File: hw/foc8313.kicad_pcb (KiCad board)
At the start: 4 copper layers, 35 x 35 mm, 146 parts, among them J1 Tag Connect, J2 Encoder, J3 CAN, J4 CAN, J6 GPIO, SW1 SW_SPST, SW2 SW_SPST, U1 LMR36015SFBRNXR, U12 TJA1051TK/3,118, U2 XC6206P332MR, U3 DRV8313PWP, U4 STM32F103CBTx, U5 AS5047D, U6 ZD24C08AE1-STGMT, U7 INA240A2D, U8 INA240A2D, X1 X322516MLB4SI

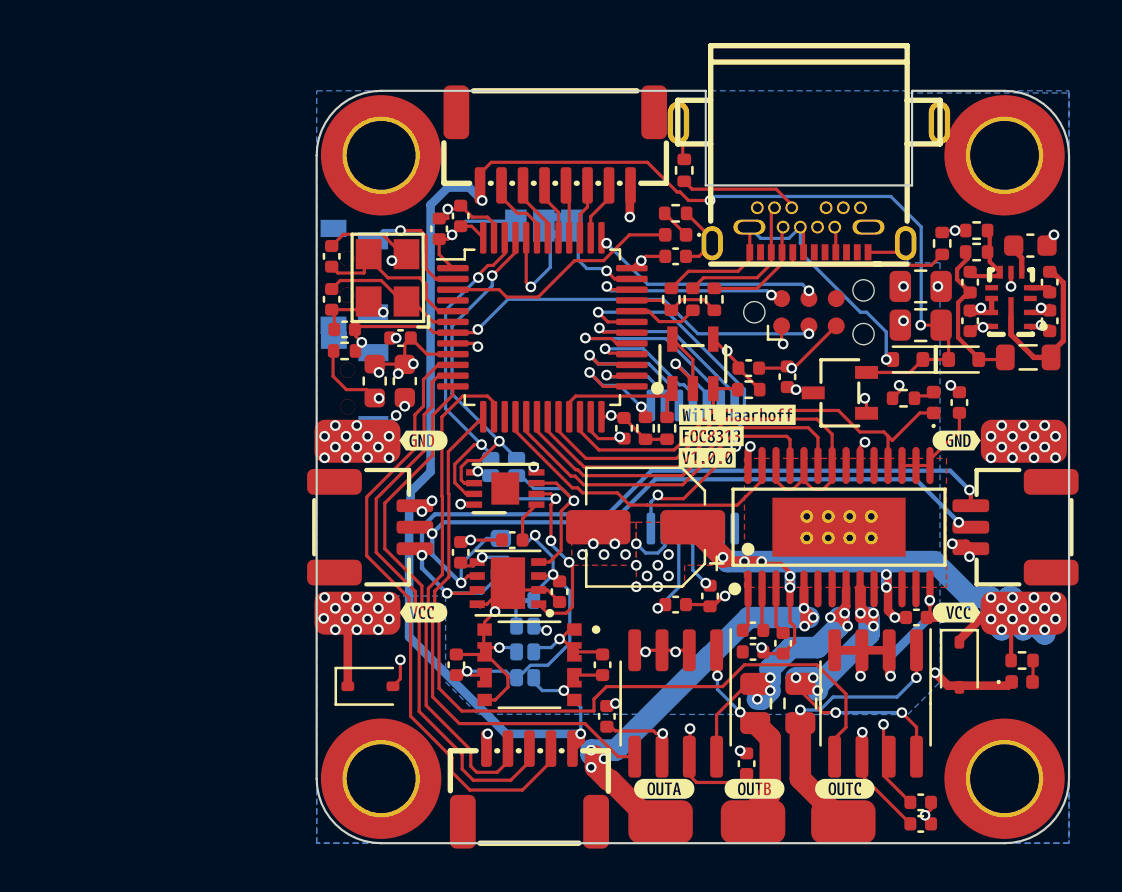
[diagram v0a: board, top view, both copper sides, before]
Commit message: [Hw] All connections completed - only DRC left
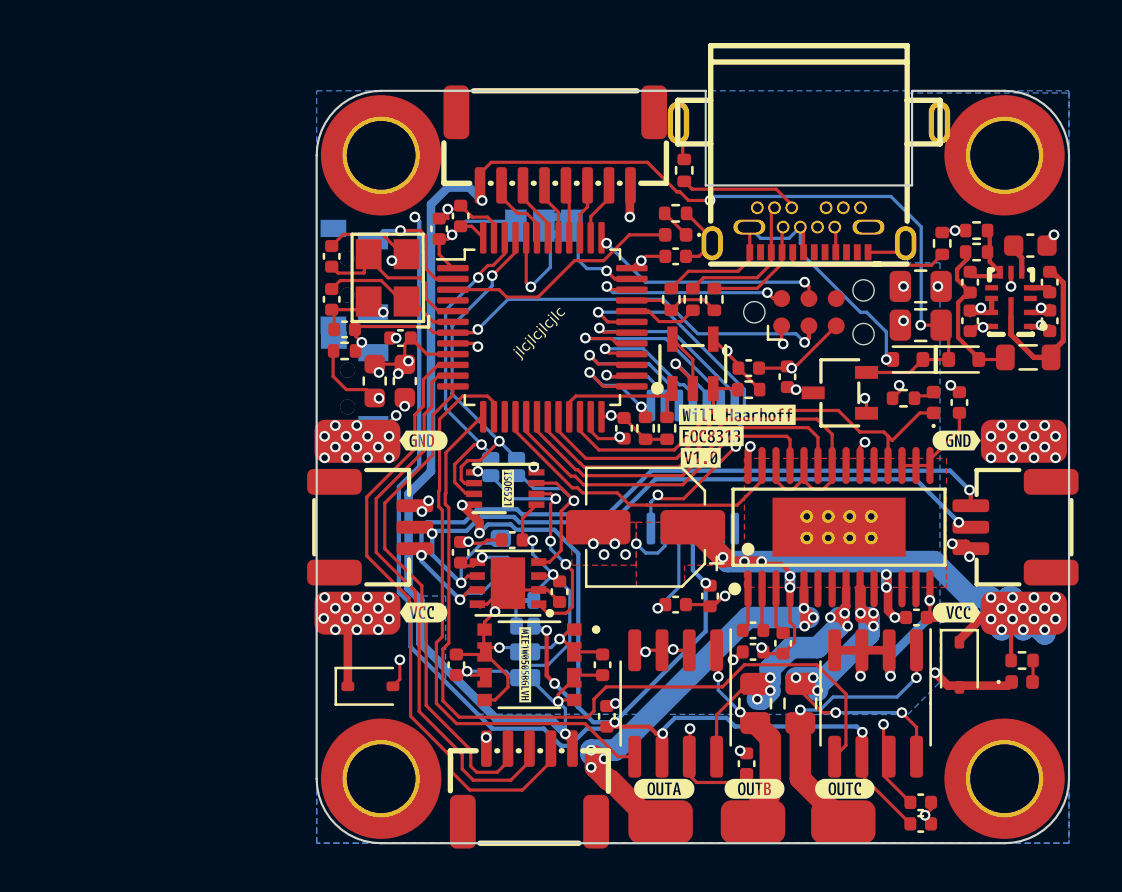
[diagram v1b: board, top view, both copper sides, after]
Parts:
- removed kibuzzard-66359B89: G***, kibuzzard-66359B89
- added kibuzzard-6635FB63: G***, kibuzzard-6635FB63, B.Cu at (133.5, 115.8)
- added kibuzzard-6635FB77: G***, kibuzzard-6635FB77, B.Cu at (132.5, 115.8)
- added kibuzzard-6635FB7E: G***, kibuzzard-6635FB7E, B.Cu at (131.5, 115.8)
- added kibuzzard-6635FC0D: G***, kibuzzard-6635FC0D, B.Cu at (156.0, 105.4)
- added kibuzzard-6635FC0D: G***, kibuzzard-6635FC0D, B.Cu at (123.9, 105.4)
- added kibuzzard-6635FC16: G***, kibuzzard-6635FC16, B.Cu at (124.1, 100.2)
- added kibuzzard-6635FC16: G***, kibuzzard-6635FC16, B.Cu at (156.0, 100.2)
- added kibuzzard-6635FD18: G***, kibuzzard-6635FD18, F.Cu at (140.4, 99.6)
- added kibuzzard-663606F1: G***, kibuzzard-663606F1, F.Cu at (132.2, 109.2)
- added kibuzzard-6636082D: G***, kibuzzard-6636082D, F.Cu at (131.4, 101.0)
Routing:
- net +3.3V: track 35.7 -> 108.5 mm, vias 12 -> 16
- net +5V: track 75.5 -> 74.5 mm
- net /~{NRST}: track 24.6 -> 25.4 mm
- net GND: track 80.1 -> 80.7 mm
- net VCC: vias 47 -> 40
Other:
- board text added: "Version 1.0"
- board text added: "jlcjlcjlcjlc"
- board text removed: "Version 1.0.0"

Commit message: [Hw] Optimised components for JLC basic parts
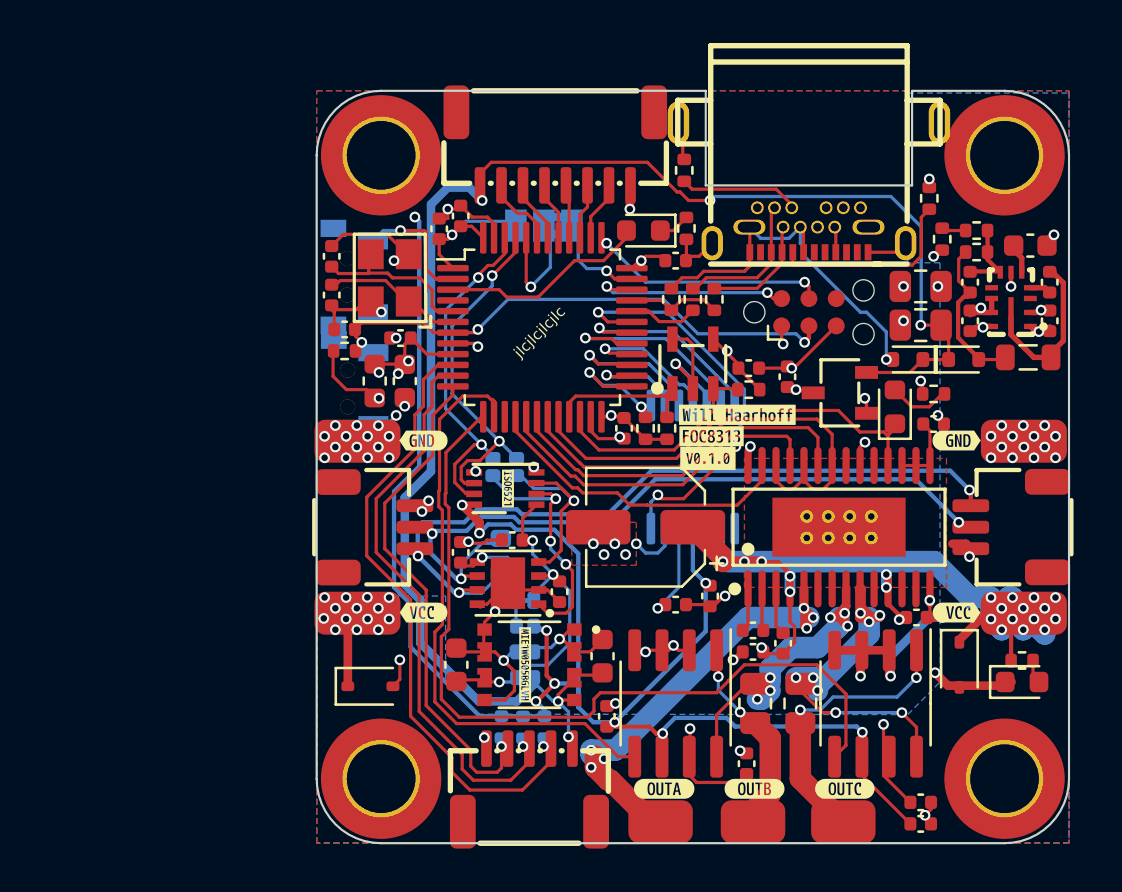
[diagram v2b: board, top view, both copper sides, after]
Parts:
- removed kibuzzard-6635FD18: G***, kibuzzard-6635FD18
- added R18: 4.7k, Resistor_SMD:R_0402_1005Metric, F.Cu at (153.2, 89.0)
- added R19: 5.1k, Resistor_SMD:R_0402_1005Metric, B.Cu at (133.1, 112.1)
- added R20: 5.1k, Resistor_SMD:R_0402_1005Metric, B.Cu at (132.1, 112.1)
- added R21: 5.1k, Resistor_SMD:R_0402_1005Metric, B.Cu at (131.1, 112.1)
- added kibuzzard-667F5C34: G***, kibuzzard-667F5C34, F.Cu at (140.7, 99.6)
- C13: value 5.1p -> 4.7p
- C37, C38: value 22uF -> 22u; footprint Capacitor_SMD:C_0402_1005Metric -> Capacitor_SMD:C_0603_1608Metric
- C8: value 470n -> 220n
- D4: footprint Diode_SMD:D_0402_1005Metric -> Diode_SMD:D_0603_1608Metric
- D5: value BLUE -> WHITE; footprint LED_SMD:LED_0402_1005Metric -> LED_SMD:LED_0603_1608Metric
- D7: value GREEN -> YELLOW; footprint LED_SMD:LED_0402_1005Metric -> LED_SMD:LED_0603_1608Metric
- R4: value 24.9k -> 20k
- U10: value ~ -> ISO6521
- moved R14 2.18 mm to (151.0, 87.5)
- moved D4 1.81 mm to (149.4, 97.2)
- moved R4 1.65 mm to (151.6, 89.4), turned to -90 degrees
- moved C8 1.56 mm to (151.2, 98.0), turned to 0 degrees
- moved D5 1.51 mm to (137.7, 89.0)
- moved R6 1.41 mm to (151.2, 96.6)
- moved R8 0.86 mm to (139.7, 88.9), turned to -90 degrees
- moved C37 0.40 mm to (135.8, 108.8)
- moved C16 0.20 mm to (123.2, 92.0)
- moved C3 0.20 mm to (139.2, 90.4)
- moved X1 0.10 mm to (125.9, 91.2)
- moved JP6 0.10 mm to (130.7, 100.0)
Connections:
- R4 pad 1: Net-(U1-FB) -> Net-(R18-Pad2)
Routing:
- net /~{DRV_NFAULT}: track 22.1 -> 20.1 mm
- net Net-(D4-A): track 1.07 -> 3.02 mm
- net /STATUS: track 11.2 -> 9.55 mm
- net +3.3V: track 108.5 -> 107.1 mm, vias 16 -> 17
- net Net-(USB1-CC1): track 7.72 -> 9.04 mm
- net +5V: track 74.5 -> 73.2 mm
- net GND: track 80.7 -> 82.0 mm, vias 71 -> 73
- net /PHC: track 19.7 -> 21.0 mm
- net /ENC2_A: track 28.7 -> 29.8 mm, vias 0 -> 1
- net /~{DRV_NRST}: track 4.32 -> 3.36 mm
- net Net-(R18-Pad2): track 0.00 -> 0.94 mm
- net /ENC2_B: track 26.1 -> 27.0 mm, vias 0 -> 1
- net /isocan/ISO5V: track 17.6 -> 16.8 mm
- net /ENC2_Z: track 23.3 -> 24.0 mm, vias 0 -> 1
- net /CAN.GND: track 19.9 -> 20.1 mm, vias 8 -> 7
- removed copper zone on F.Cu, net VCC
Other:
- board text added: "Version 0.1.0"
- board text removed: "Version 1.0"

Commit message: [Hw] Version 0.1.0 - sent for manufacture
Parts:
- added R22: 5.1k, Resistor_SMD:R_0402_1005Metric, B.Cu at (132.7, 94.6)
- added R23: 5.1k, Resistor_SMD:R_0402_1005Metric, B.Cu at (132.7, 95.6)
- added R24: 5.1k, Resistor_SMD:R_0402_1005Metric, B.Cu at (132.7, 93.6)
- SW1, SW2: footprint easyeda:SW-SMD_L4.7-W3.5-P3.35-EH -> easyeda:SW-TH_PANASONIC_EVPAKE31A
- U10: value ISO6521 -> ISO6521F
- moved kibuzzard-66359642 2.07 mm to (127.7, 94.1)
- moved kibuzzard-6635961B 1.97 mm to (127.4, 89.4)
- moved C7 1.43 mm to (123.5, 95.0)
- moved R1 1.43 mm to (123.5, 96.0)
- moved SW2 1.07 mm to (124.0, 95.3)
- moved SW1 0.69 mm to (124.0, 90.5)
- moved C16 0.67 mm to (123.5, 91.4), turned to 0 degrees
- moved C2 0.32 mm to (128.2, 88.6)
- moved C17 0.30 mm to (123.5, 90.2), turned to 180 degrees
- moved R7 0.20 mm to (155.3, 108.8)
- moved C26 0.20 mm to (150.4, 116.6)
- moved C27 0.20 mm to (150.4, 115.6)
- moved X1 0.20 mm to (126.1, 91.2)
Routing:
- net GND: track 82.0 -> 86.5 mm, vias 73 -> 75
- net +3.3V: track 107.1 -> 110.4 mm, vias 17 -> 22
- net /ENC1_A: track 9.71 -> 12.7 mm
- net /ENC1_Z: track 19.3 -> 22.0 mm
- net /ENC1_B: track 10.2 -> 12.6 mm
- net +3.3VA: track 14.3 -> 16.0 mm
- net +5V: track 73.2 -> 74.7 mm
- net /HSE_IN: track 7.83 -> 6.79 mm
- net /HSE_OUT: track 6.54 -> 5.87 mm
- net /~{BTN}: track 5.84 -> 6.45 mm
- net /CAN.GND: vias 7 -> 8

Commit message: [Hw] WIP begun revisions for v0.2.0
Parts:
- removed D2: RB521S30T1G, Diode_SMD:D_SOD-523
- added R25: 100k, Resistor_SMD:R_0402_1005Metric, F.Cu at (114.5, 98.0)
- added R26: 10k, Resistor_SMD:R_0402_1005Metric, F.Cu at (114.5, 100.0)
- C13: value 4.7p -> 100n
- R12, R13: value 6m -> 10m
- moved C13 43.4 mm to (111.5, 104.6), turned to 0 degrees
- moved D6 4.34 mm to (152.1, 91.2)
- moved C9 3.20 mm to (150.6, 94.8)
- moved L2 1.40 mm to (154.2, 95.0)
- moved C14 0.60 mm to (150.6, 92.8)
- moved C11 0.30 mm to (152.9, 92.9)
- moved J1 0.20 mm to (145.4, 93.0)
- turned C12 to 90 degrees
- turned C15 to 180 degrees
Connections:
- C12 pad 1: Net-(U1-SW) -> Net-(U1-NC)
- C13 pad 1: Net-(D2-A) -> /VSENSE
- C13 pad 2: Net-(U1-FB) -> GND
- C33 pad 2: /CAN.GND -> Net-(U12-EP)
- C34 pad 2: /CAN.GND -> Net-(U12-EP)
- C35 pad 2: /CAN.GND -> Net-(U12-EP)
- C38 pad 2: /CAN.GND -> Net-(U12-EP)
- J1 pad 1: +3V3 -> +3.3V
- L2 pad 1: Net-(D2-A) -> +5V
- L2 pad 2: Net-(U1-SW) -> Net-(U1-NC)
- PS1 pad 2: /CAN.GND -> Net-(U12-EP)
- PS1 pad 3_4: /CAN.GND -> Net-(U12-EP)
- PS1 pad 7: /CAN.GND -> unconnected-(PS1-VSEL-Pad7)
- R3 pad 1: Net-(D2-A) -> +5V
- U1 pad 12: Net-(U1-SW) -> Net-(U1-NC)
- U1 pad 3: unconnected-(U1-NC-Pad3) -> Net-(U1-NC)
- U10 pad 4: /CAN.GND -> Net-(U12-EP)
- U12 pad 2: /CAN.GND -> Net-(U12-EP)
- U12 pad 8: /CAN.GND -> Net-(U12-EP)
- U12 pad 9: /CAN.GND -> Net-(U12-EP)
- U2 pad 2: +5V -> +3.3V
- U2 pad 3: +3.3V -> +5V
- U4 pad 15: unconnected-(U4-PA5-Pad15) -> /VSENSE
- USB1 pad A10: /USB_DM_EXT -> unconnected-(USB1-SSRXN2-PadA10)
- USB1 pad A12: +5VD -> GND
- USB1 pad A4: GND -> +5VD
- USB1 pad A5: unconnected-(USB1-SSTXP1-PadA5) -> Net-(USB1-CC1)
- USB1 pad A6: unconnected-(USB1-SSTXN1-PadA6) -> /USB_DP_EXT
- USB1 pad A7: +5VD -> /USB_DM_EXT
- USB1 pad A8: Net-(USB1-CC1) -> unconnected-(USB1-SBU1-PadA8)
- USB1 pad A9: /USB_DP_EXT -> +5VD
- USB1 pad B1: +5VD -> GND
- USB1 pad B11: GND -> unconnected-(USB1-SSRXP1-PadB11)
- USB1 pad B12: unconnected-(USB1-SSRXN1-PadB12) -> GND
- USB1 pad B3: /USB_DM_EXT -> unconnected-(USB1-SSTXN2-PadB3)
- USB1 pad B4: /USB_DP_EXT -> +5VD
- USB1 pad B6: +5VD -> /USB_DP_EXT
- USB1 pad B7: unconnected-(USB1-SSTXN2-PadB7) -> /USB_DM_EXT
- USB1 pad B9: GND -> +5VD
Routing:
- net /CAN.GND: track 20.1 -> 3.60 mm, vias 8 -> 4
- net Net-(U12-EP): track 0.00 -> 11.7 mm, vias 0 -> 3
- net Net-(U1-SW): track 7.77 -> 0.00 mm
- net Net-(D2-A): track 7.14 -> 0.00 mm
- net Net-(USB1-CC2): track 5.45 -> 0.52 mm
- net Net-(U1-NC): track 0.00 -> 4.92 mm
- net GND: track 86.5 -> 90.4 mm, vias 75 -> 74
- net VCC: track 52.9 -> 56.4 mm, vias 40 -> 41
- net +3.3V: track 110.4 -> 112.9 mm, vias 22 -> 20
- net /USB_DP_EXT: track 5.35 -> 7.71 mm, vias 0 -> 1
- net +5VD: track 17.9 -> 20.1 mm
- net /SWDIO: track 9.59 -> 11.4 mm
- net +5V: track 74.7 -> 76.5 mm, vias 5 -> 6
- net Net-(USB1-CC1): track 9.04 -> 7.62 mm
- net Net-(U1-FB): track 3.65 -> 2.23 mm
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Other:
- outline, holes or cut-outs redrawn

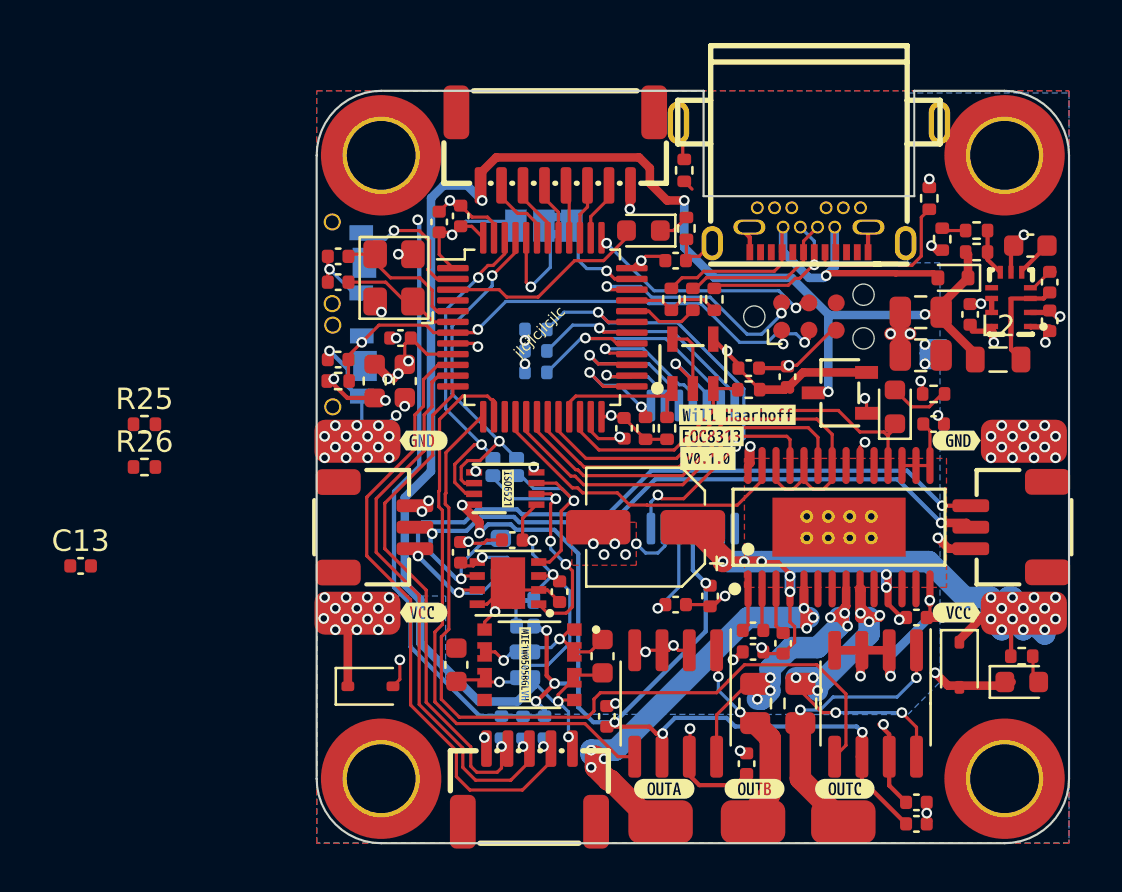
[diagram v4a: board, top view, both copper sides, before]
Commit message: [Hw] Unpinched Vcc to 3.4mm width
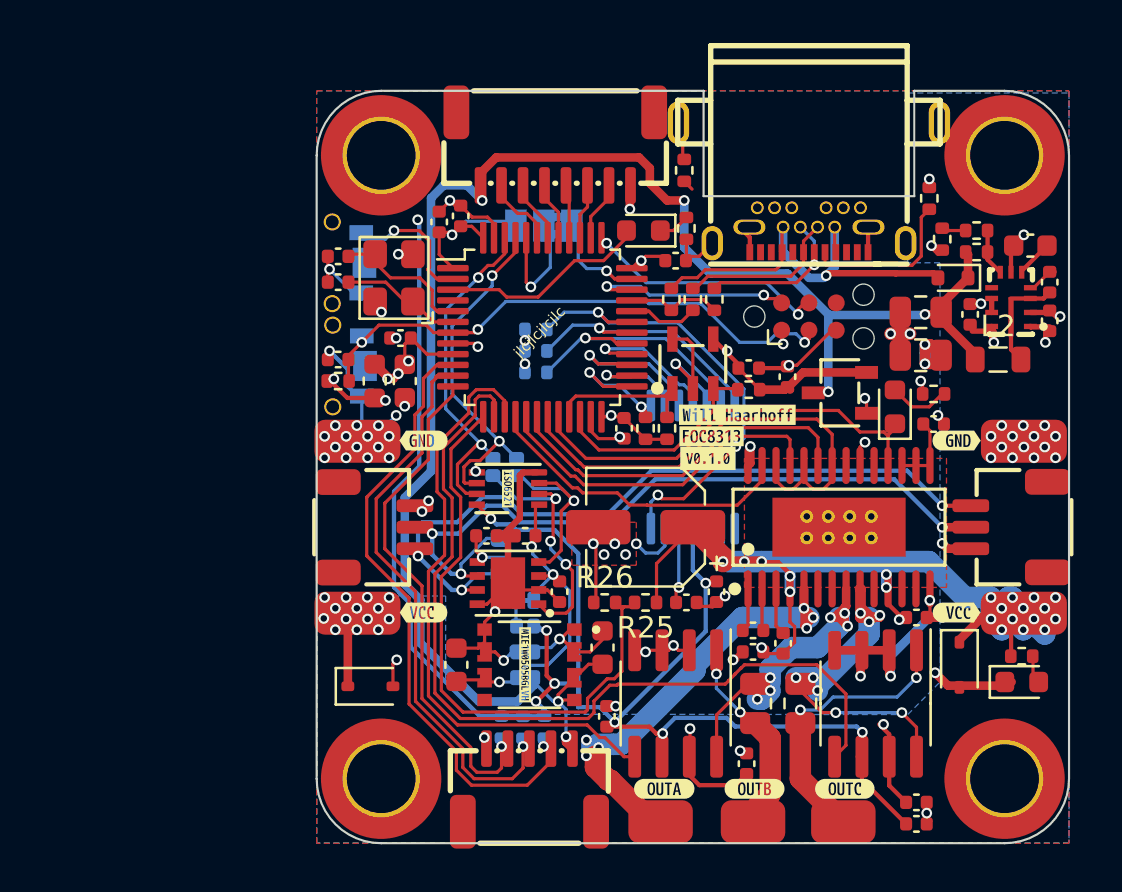
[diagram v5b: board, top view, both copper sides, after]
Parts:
- removed C13: 100n, Capacitor_SMD:C_0402_1005Metric
- moved R25 24.7 mm to (137.8, 106.3), turned to 180 degrees
- moved R26 22.3 mm to (135.9, 106.3)
- moved C34 1.43 mm to (130.4, 103.2), turned to 0 degrees
- moved C35 0.63 mm to (132.2, 103.2)
- moved C24 0.51 mm to (139.7, 106.3)
- moved C37 0.40 mm to (135.8, 108.4)
- moved C36 0.36 mm to (141.1, 105.8)
- moved U10 0.12 mm to (131.4, 101.0)
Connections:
- C33 pad 2: Net-(U12-EP) -> /CAN.GND
- C34 pad 2: Net-(U12-EP) -> /CAN.GND
- C35 pad 2: Net-(U12-EP) -> /CAN.GND
- C38 pad 2: Net-(U12-EP) -> /CAN.GND
- PS1 pad 2: Net-(U12-EP) -> /CAN.GND
- PS1 pad 3_4: Net-(U12-EP) -> /CAN.GND
- U10 pad 4: Net-(U12-EP) -> /CAN.GND
- U12 pad 2: Net-(U12-EP) -> /CAN.GND
- U12 pad 8: Net-(U12-EP) -> /CAN.GND
- U12 pad 9: Net-(U12-EP) -> /CAN.GND
- U4 pad 13: /ISENSE_C -> /VSENSE
- U4 pad 14: /ISENSE_B -> /ISENSE_C
- U4 pad 15: /VSENSE -> /ISENSE_B
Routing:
- net /VSENSE: track 0.00 -> 27.6 mm
- net /CAN.GND: track 3.60 -> 21.4 mm, vias 4 -> 5
- net Net-(U12-EP): track 11.7 -> 0.00 mm, vias 3 -> 0
- net VCC: track 56.4 -> 60.9 mm
- net GND: track 90.4 -> 93.6 mm
- net /ISENSE_C: track 38.3 -> 41.2 mm
- net /SWDIO: track 11.4 -> 9.59 mm
- net +3.3V: track 112.9 -> 111.5 mm, vias 20 -> 19
- net /ISENSE_B: track 27.5 -> 28.5 mm
- net /OUTA: track 21.3 -> 22.1 mm
- net Net-(U5-VDD3V3): track 4.11 -> 3.49 mm
